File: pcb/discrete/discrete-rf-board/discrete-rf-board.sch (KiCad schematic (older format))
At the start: 22 parts, among them J1 Conn_01x11, J2 Conn_01x26, J3 Conn_01x30, J4 UFL, J5 UFL, J6 SMA, U1 BGS12PL6E6327XTSA1, U2 BGS12PL6E6327XTSA1

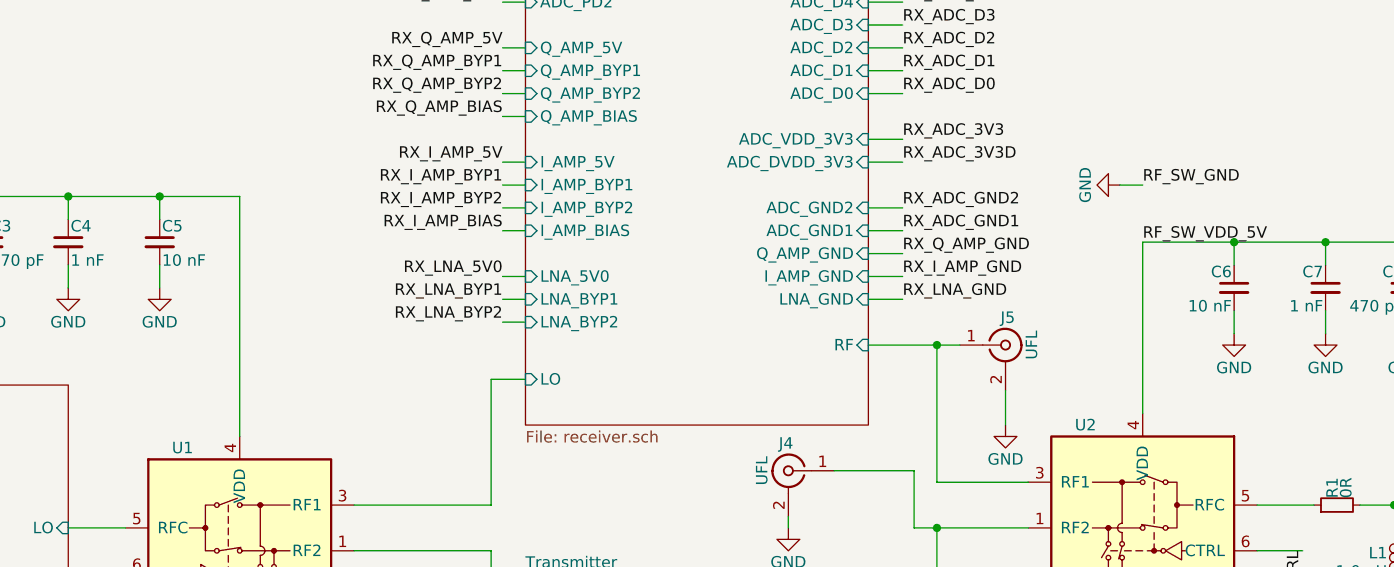
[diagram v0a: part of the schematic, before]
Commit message: Add more footprints, saving before autofill
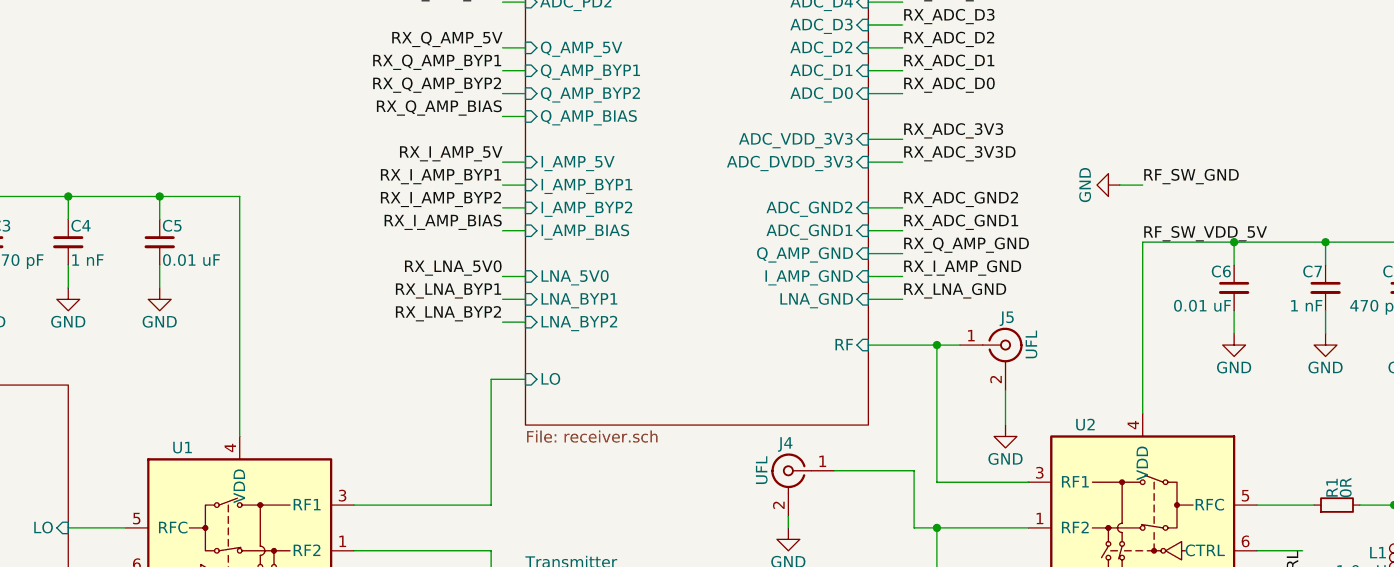
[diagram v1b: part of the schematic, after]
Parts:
- C5: value 10 nF -> 0.01 uF; footprint (none) -> Capacitor_SMD:C_0402_1005Metric; Mouser (none) -> 80-C0402C103K4R7411
- C6: value 10 nF -> 0.01 uF
- L1: footprint (none) -> Capacitor_SMD:C_0402_1005Metric; Mouser (none) -> 810-MLG1005S1N0ST000
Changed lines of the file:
@@
 F 0 "L1" H 9430 3540 50  0000 L CNN
 F 1 "1.0 nH" H 9430 3460 50  0000 L CNN
-F 2 "" H 9400 3500 50  0001 C CNN
+F 2 "Capacitor_SMD:C_0402_1005Metric" H 9400 3500 50  0001 C CNN
 F 3 "~" H 9400 3500 50  0001 C CNN
+F 4 "810-MLG1005S1N0ST000" H 9400 3500 50  0001 C CNN "Mouser"
 	1    9400 3500
 	-1   0    0    -1
@@
 P 4000 2100
 F 0 "C5" H 4010 2170 50  0000 L CNN
-F 1 "10 nF" H 4010 2020 50  0000 L CNN
-F 2 "" H 4000 2100 50  0001 C CNN
+F 1 "0.01 uF" H 4010 2020 50  0000 L CNN
+F 2 "Capacitor_SMD:C_0402_1005Metric" H 4000 2100 50  0001 C CNN
 F 3 "~" H 4000 2100 50  0001 C CNN
+F 4 "80-C0402C103K4R7411" H 4000 2100 50  0001 C CNN "Mouser"
 	1    4000 2100
 	1    0    0    -1
@@
 P 8700 2300
 F 0 "C6" H 8710 2370 50  0000 L CNN
-F 1 "10 nF" H 8710 2220 50  0000 L CNN
+F 1 "0.01 uF" H 8710 2220 50  0000 L CNN
 F 2 "" H 8700 2300 50  0001 C CNN
 F 3 "~" H 8700 2300 50  0001 C CNN

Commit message: Autofill
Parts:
- C6: footprint (none) -> Capacitor_SMD:C_0402_1005Metric; Mouser (none) -> 80-C0402C103K4R7411
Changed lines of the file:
@@
 F 0 "C6" H 8710 2370 50  0000 L CNN
 F 1 "0.01 uF" H 8710 2220 50  0000 L CNN
-F 2 "" H 8700 2300 50  0001 C CNN
+F 2 "Capacitor_SMD:C_0402_1005Metric" H 8700 2300 50  0001 C CNN
 F 3 "~" H 8700 2300 50  0001 C CNN
+F 4 "80-C0402C103K4R7411" H 8700 2300 50  0001 C CNN "Mouser"
 	1    8700 2300
 	-1   0    0    -1

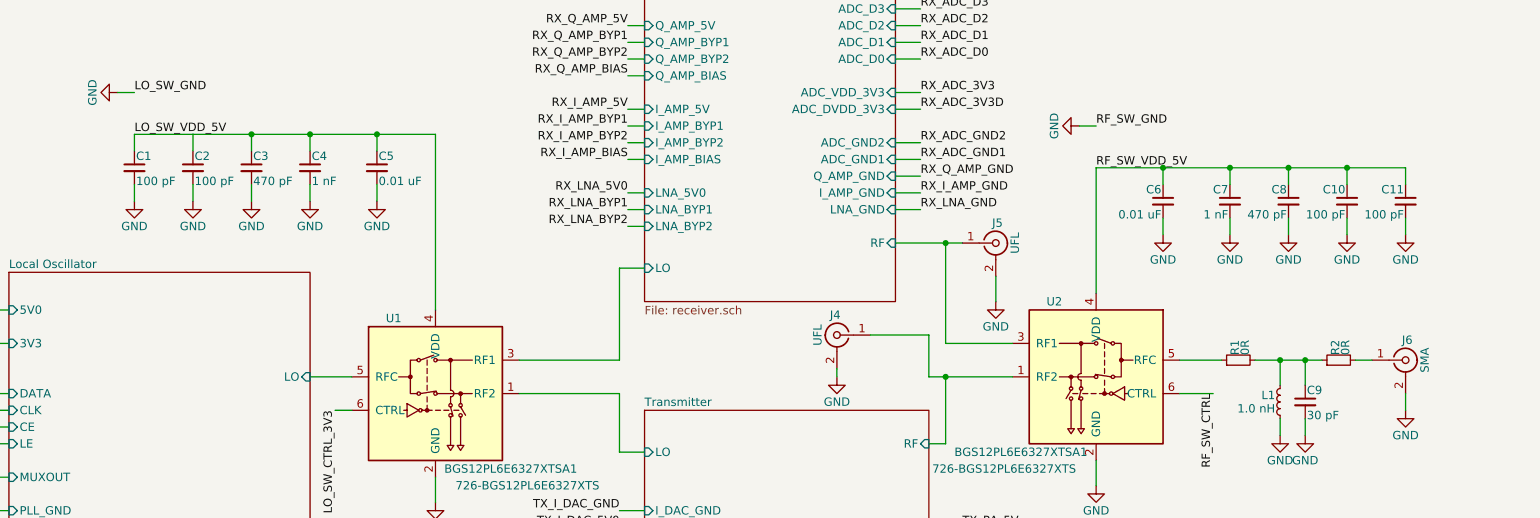
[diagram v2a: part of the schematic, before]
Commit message: Reannotate everything; I'm trying to cut down the number of components
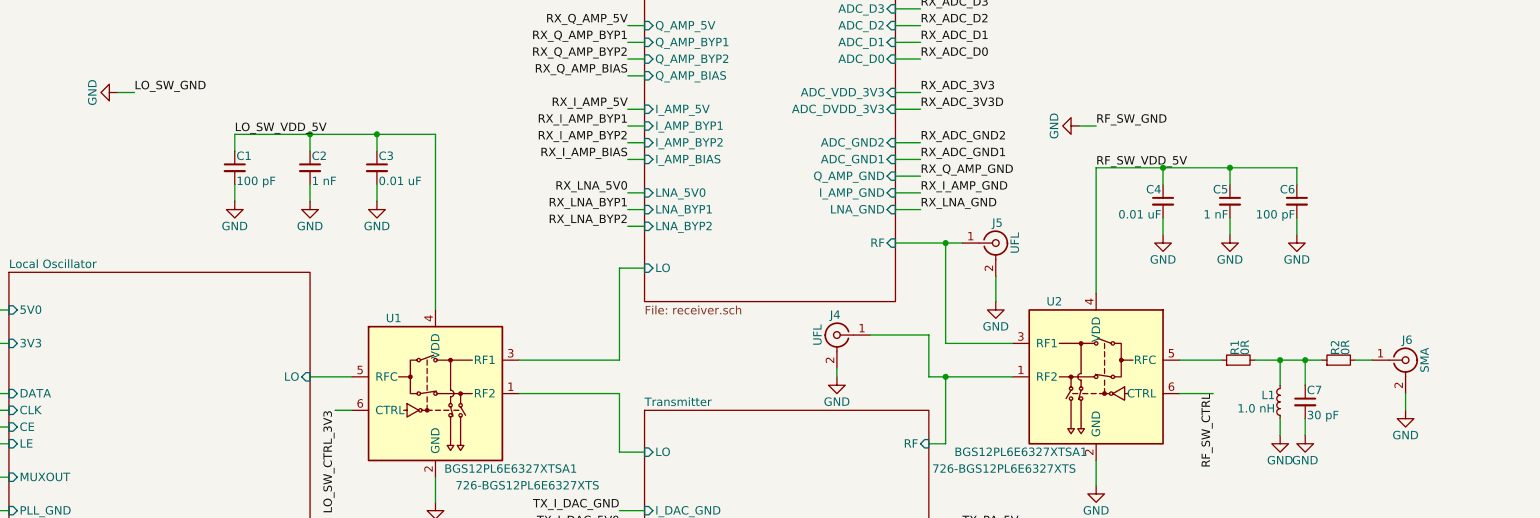
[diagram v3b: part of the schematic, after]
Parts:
- removed C11, C2: 100 pF, Capacitor_SMD:C_0402_1005Metric, symbol Device:C_Small
- removed C3, C8: 470 pF, symbol Device:C_Small
- renumbered C4 to C2, C5 to C3, C6 to C4, C7 to C5, C10 to C6, C9 to C7
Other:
- moved on the sheet: C1, C6

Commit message: Footprint a lot of stuff; save before autofill
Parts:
- C2: footprint (none) -> Capacitor_SMD:C_0402_1005Metric; Mouser (none) -> 80-C0402C102K5R7411
- C7: footprint (none) -> Capacitor_SMD:C_0402_1005Metric; Mouser (none) -> 81-GCM1555C1H300FA6D
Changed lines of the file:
@@
 F 0 "C7" H 9560 3570 50  0000 L CNN
 F 1 "30 pF" H 9560 3420 50  0000 L CNN
-F 2 "" H 9550 3500 50  0001 C CNN
+F 2 "Capacitor_SMD:C_0402_1005Metric" H 9550 3500 50  0001 C CNN
 F 3 "~" H 9550 3500 50  0001 C CNN
+F 4 "81-GCM1555C1H300FA6D" H 9550 3500 50  0001 C CNN "Mouser"
 	1    9550 3500
 	1    0    0    -1
@@
 F 0 "C2" H 3610 2170 50  0000 L CNN
 F 1 "1 nF" H 3610 2020 50  0000 L CNN
-F 2 "" H 3600 2100 50  0001 C CNN
+F 2 "Capacitor_SMD:C_0402_1005Metric" H 3600 2100 50  0001 C CNN
 F 3 "~" H 3600 2100 50  0001 C CNN
+F 4 "80-C0402C102K5R7411" H 3600 2100 50  0001 C CNN "Mouser"
 	1    3600 2100
 	1    0    0    -1

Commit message: Autofill
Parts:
- C5: footprint (none) -> Capacitor_SMD:C_0402_1005Metric; Mouser (none) -> 80-C0402C102K5R7411
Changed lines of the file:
@@
 F 0 "C5" H 9110 2370 50  0000 L CNN
 F 1 "1 nF" H 9110 2220 50  0000 L CNN
-F 2 "" H 9100 2300 50  0001 C CNN
+F 2 "Capacitor_SMD:C_0402_1005Metric" H 9100 2300 50  0001 C CNN
 F 3 "~" H 9100 2300 50  0001 C CNN
+F 4 "80-C0402C102K5R7411" H 9100 2300 50  0001 C CNN "Mouser"
 	1    9100 2300
 	-1   0    0    -1

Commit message: Add in a couple more components, save before autofill
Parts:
- J1, J2, J3: Mouser (none) -> NoPart
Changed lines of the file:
@@
 F 2 "" H 3400 6150 50  0001 C CNN
 F 3 "~" H 3400 6150 50  0001 C CNN
+F 4 "NoPart" H 3400 6150 50  0001 C CNN "Mouser"
 	1    3400 6150
 	-1   0    0    -1
@@
 F 2 "" H 950 5850 50  0001 C CNN
 F 3 "~" H 950 5850 50  0001 C CNN
+F 4 "NoPart" H 950 5850 50  0001 C CNN "Mouser"
 	1    950  5850
 	-1   0    0    -1
@@
 F 2 "" H 2100 6000 50  0001 C CNN
 F 3 "~" H 2100 6000 50  0001 C CNN
+F 4 "NoPart" H 2100 6000 50  0001 C CNN "Mouser"
 	1    2100 6000
 	-1   0    0    -1
